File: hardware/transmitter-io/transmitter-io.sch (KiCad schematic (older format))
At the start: 14 parts, among them J1 Output, J2 INPUT, J3 IO EXTENSION, U1 74LS07

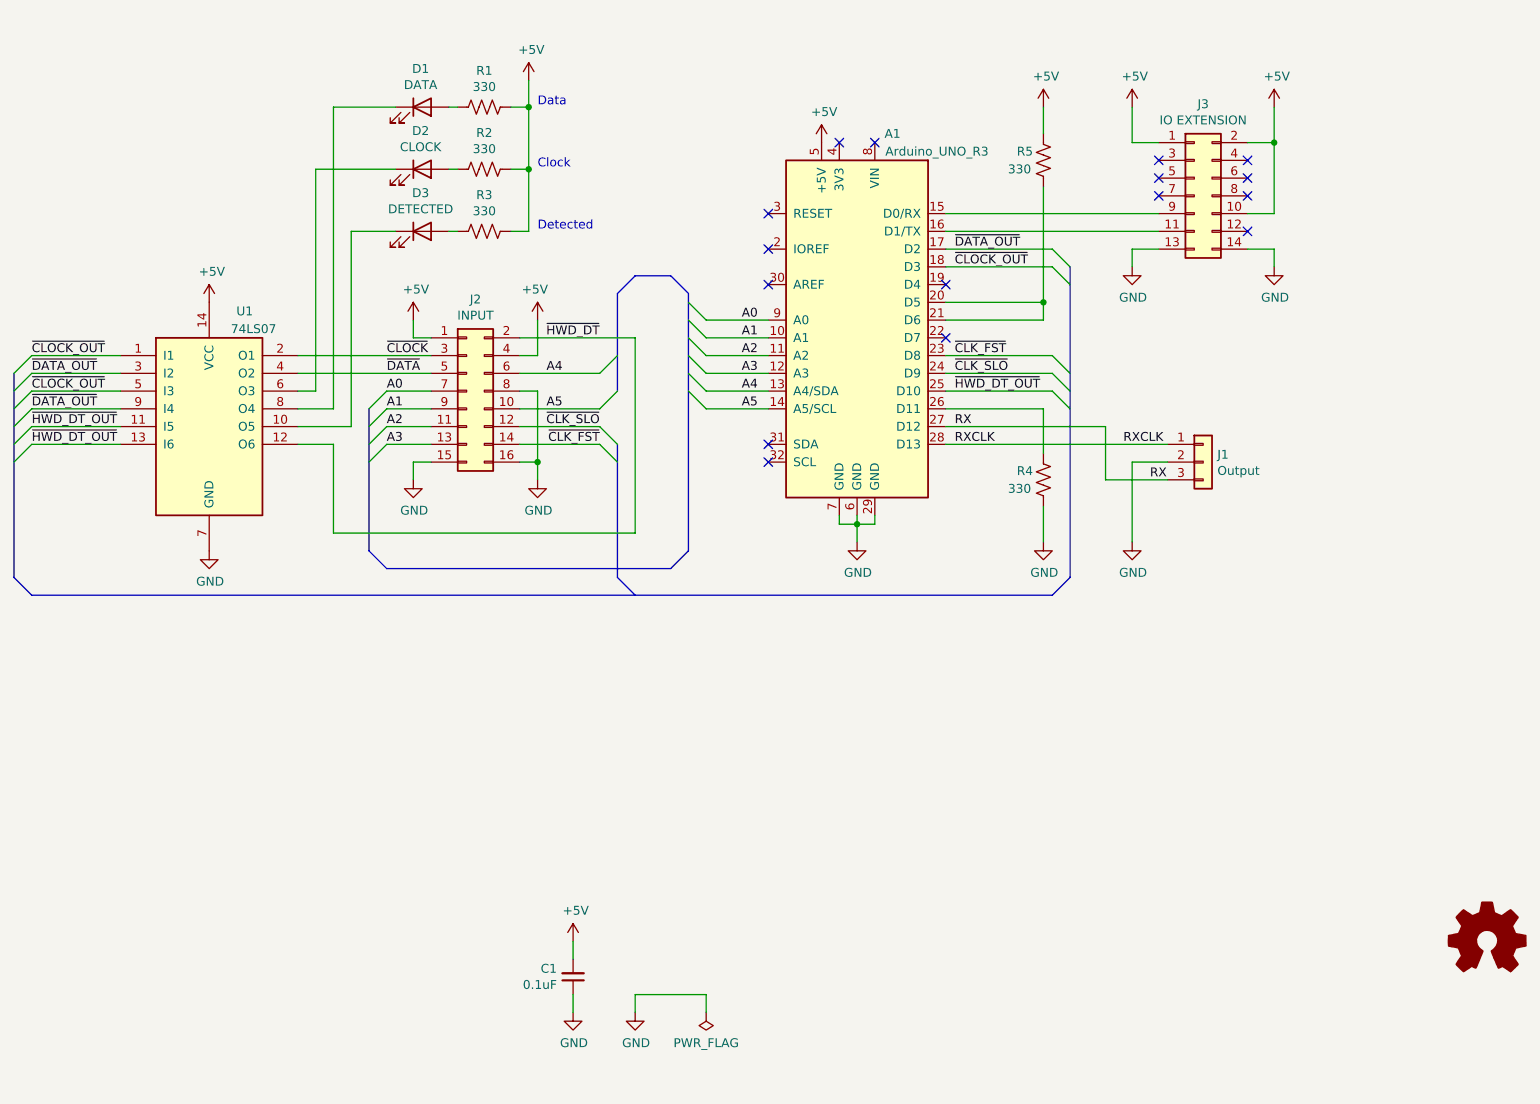
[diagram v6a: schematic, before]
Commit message: Breakup TX2 into 2 boards, allowing IO boards to be used with TX1.
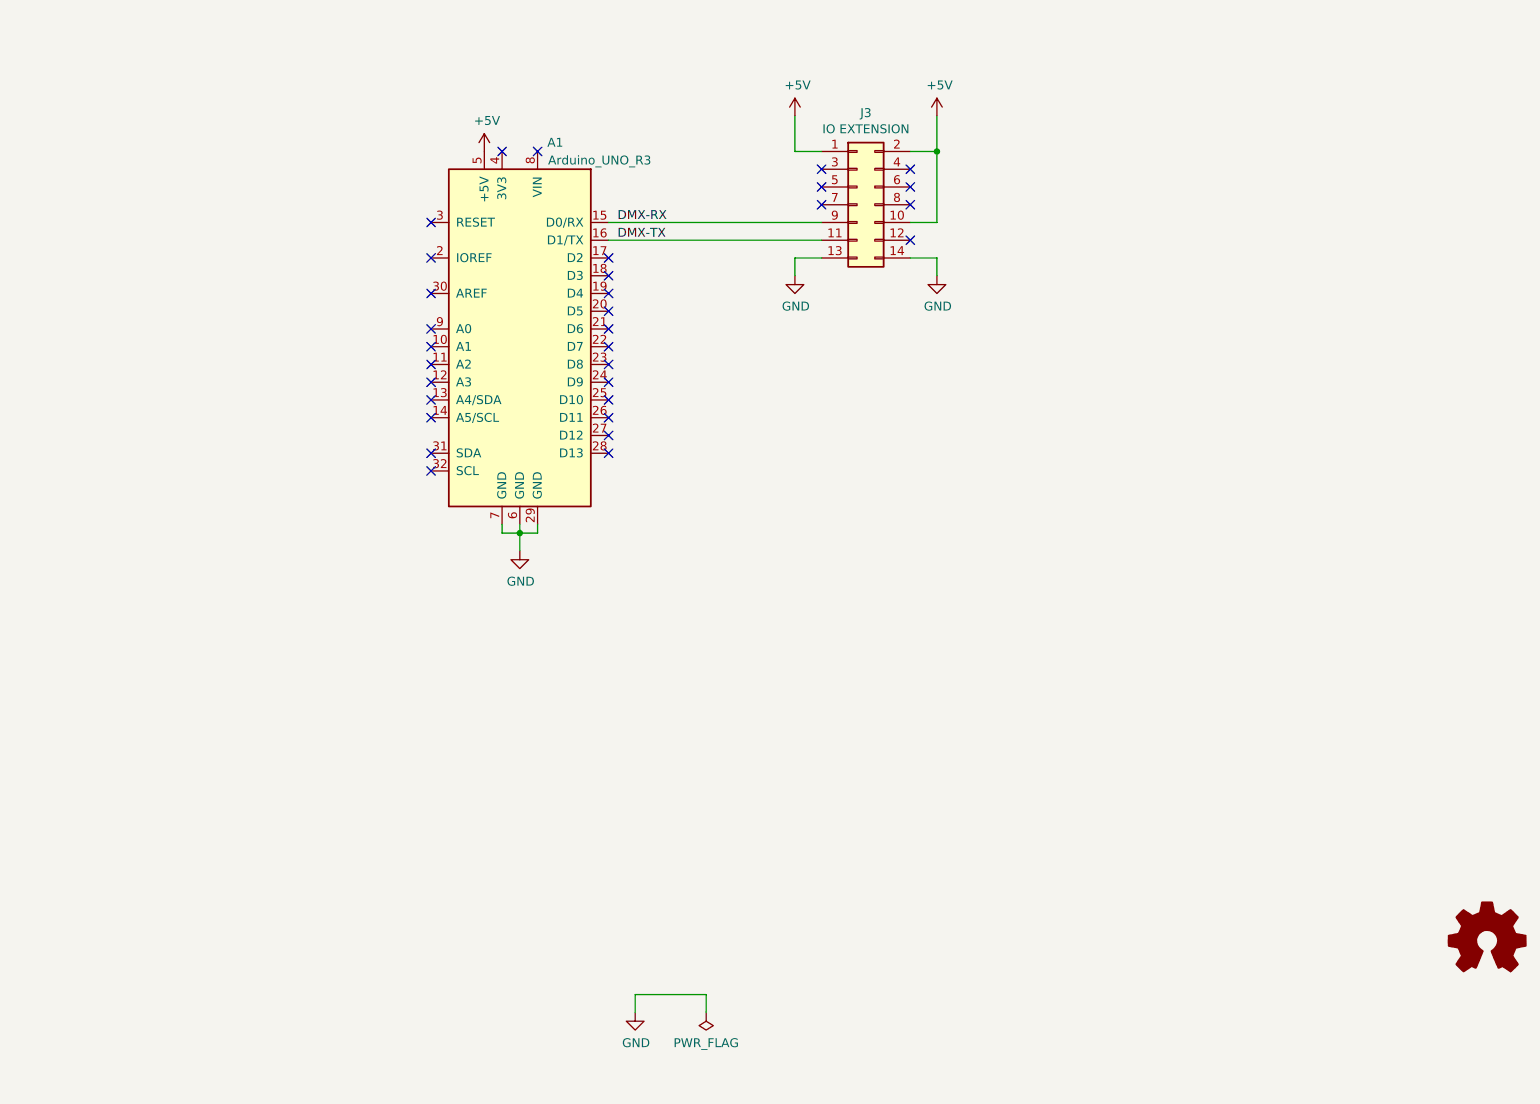
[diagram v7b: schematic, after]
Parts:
- removed C1: 0.1uF, Capacitor_THT:C_Disc_D3.0mm_W1.6mm_P2.50mm, symbol Device:C_Small
- removed D1: DATA, LED_THT:LED_D5.0mm, symbol Device:LED
- removed D2: CLOCK, LED_THT:LED_D5.0mm, symbol Device:LED
- removed D3: DETECTED, LED_THT:LED_D5.0mm, symbol Device:LED
- removed J1: Output, Connector_PinHeader_2.54mm:PinHeader_1x03_P2.54mm_Horizontal, symbol Connector_Generic:Conn_01x03
- removed J2: INPUT, Connector_IDC:IDC-Header_2x08_P2.54mm_Horizontal, symbol Connector_Generic:Conn_02x08_Odd_Even
- removed R1, R2, R3, R4, R5: 330, Resistor_THT:R_Axial_DIN0207_L6.3mm_D2.5mm_P10.16mm_Horizontal, symbol Device:R_US
- removed U1: 74LS07, Package_DIP:DIP-14_W7.62mm, symbol DMXDemonstrator:74LS07
- A1: PartId A_ARDUINO,H_ARDUINO -> H_ARDUINO
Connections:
- net DMX-RX: now reaches A1.15 (D0/RX), J3.9 (Pin_9)
- net DMX-TX: now reaches A1.16 (D1/TX), J3.11 (Pin_11)
- net at A1.20 (D5): no longer A1.21 (D6)
- net A0: no longer names the net of A1.9 (A0)
- net A1: no longer names the net of A1.10 (A1)
- net A2: no longer names the net of A1.11 (A2)
- net A3: no longer names the net of A1.12 (A3)
- net A4: no longer names the net of A1.13 (A4/SDA)
- net A5: no longer names the net of A1.14 (A5/SCL)
- net RX: no longer names the net of A1.27 (D12)
- net RXCLK: no longer names the net of A1.28 (D13)
- net ~CLK_FST: no longer names the net of A1.23 (D8)
- net ~CLK_SLO: no longer names the net of A1.24 (D9)
- net ~CLOCK_OUT: no longer names the net of A1.18 (D3)
- net ~DATA_OUT: no longer names the net of A1.17 (D2)
- net ~HWD_DT_OUT: no longer names the net of A1.25 (D10)
- no-connect marks 16 -> 32
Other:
- note removed: "Clock"
- note removed: "Data"
- note removed: "Detected"
- moved on the sheet: A1, J3
